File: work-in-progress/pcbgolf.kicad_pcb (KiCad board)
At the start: 4 copper layers, 45 x 37 mm, 239 parts, among them J1 DCBARRELSMT, J2 MICRO_SD-0472192001, J3 USB4105-GF-A, J4 CAN, J5 USB-C-FEMALEGCT, J6 USB-C-FEMALEGCT, J7 USB-C-FEMALEGCT, J8 USB-C-FEMALEGCT, Q1 SIS427-VI, Q2 NFET-DUAL-COMMON-SOURCE-QS5K2, Q3 NFET-DUAL-COMMON-SOURCE-QS5K2, Q4 NFET-DUAL-COMMON-SOURCE-QS5K2, Q5 NFET-DUAL-COMMON-SOURCE-QS5K2, Q6 NFET-DUAL-COMMON-SOURCE-QS5K2, Q7 NFET-DUAL-COMMON-SOURCE-QS5K2, Q8 NFET-DUAL-COMMON-SOURCE-QS5K2, Q9 NFET-DUAL-COMMON-SOURCE-QS5K2, SW1 SPST-2-4PIN, U1 AP62300, U10 NCS20071XV53T2G, U11 NCS20071XV53T2G, U12 NCS20071XV53T2G, U13 TPS25944A, U14 TPS25944A, U15 TPS25944A, U16 TPS25944A, U2 AP62300, U3 STM32H725VGH6, U4 USB2517, U5 MCP2542FDT-E/MNY, U6 MCP2542FDT-E/MNY, U7 MCP2542FDT-E/MNY, U8 MCP2542FDT-E/MNY, U9 NCS20071XV53T2G, Y1 25MHz, Y2 24MHz

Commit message: Advance solo completion to a checked 220-connection WIP
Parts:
- moved Y1 6.91 mm to (3.60, 15.3), turned to 180 degrees
- moved C19 6.40 mm to (4.05, 24.3)
- moved C14 2.97 mm to (3.60, 17.4), turned to 0 degrees
- moved C17 2.33 mm to (1.00, 16.3), turned to 90 degrees
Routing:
- net GND: track 22.2 -> 178.6 mm, vias 57 -> 154
- net CAN1_L: track 0.00 -> 86.8 mm, vias 0 -> 8
- net CAN3_L: track 0.00 -> 76.8 mm, vias 0 -> 5
- net CAN1_H: track 0.00 -> 67.3 mm, vias 0 -> 4
- net CAN0_H: track 0.00 -> 66.6 mm, vias 0 -> 7
- net CAN0_L: track 0.00 -> 52.9 mm, vias 0 -> 4
- net CAN3_H: track 0.00 -> 52.2 mm, vias 0 -> 5
- net Net-(U9--): track 0.00 -> 51.5 mm, vias 0 -> 5
- net BTN: track 1.60 -> 51.0 mm, vias 0 -> 2
- net Net-(Q9-D1): track 0.00 -> 48.4 mm, vias 0 -> 4
- net Net-(Q5-D1): track 0.00 -> 39.6 mm, vias 0 -> 3
- net CAN2_H: track 0.00 -> 37.8 mm, vias 0 -> 4
- net CH4_SBU2_RELAY: track 0.57 -> 36.2 mm, vias 1 -> 2
- net Net-(U3-PC0): track 0.57 -> 34.7 mm
- net CH3_SBU1_RELAY: track 0.57 -> 34.7 mm, vias 1 -> 2
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
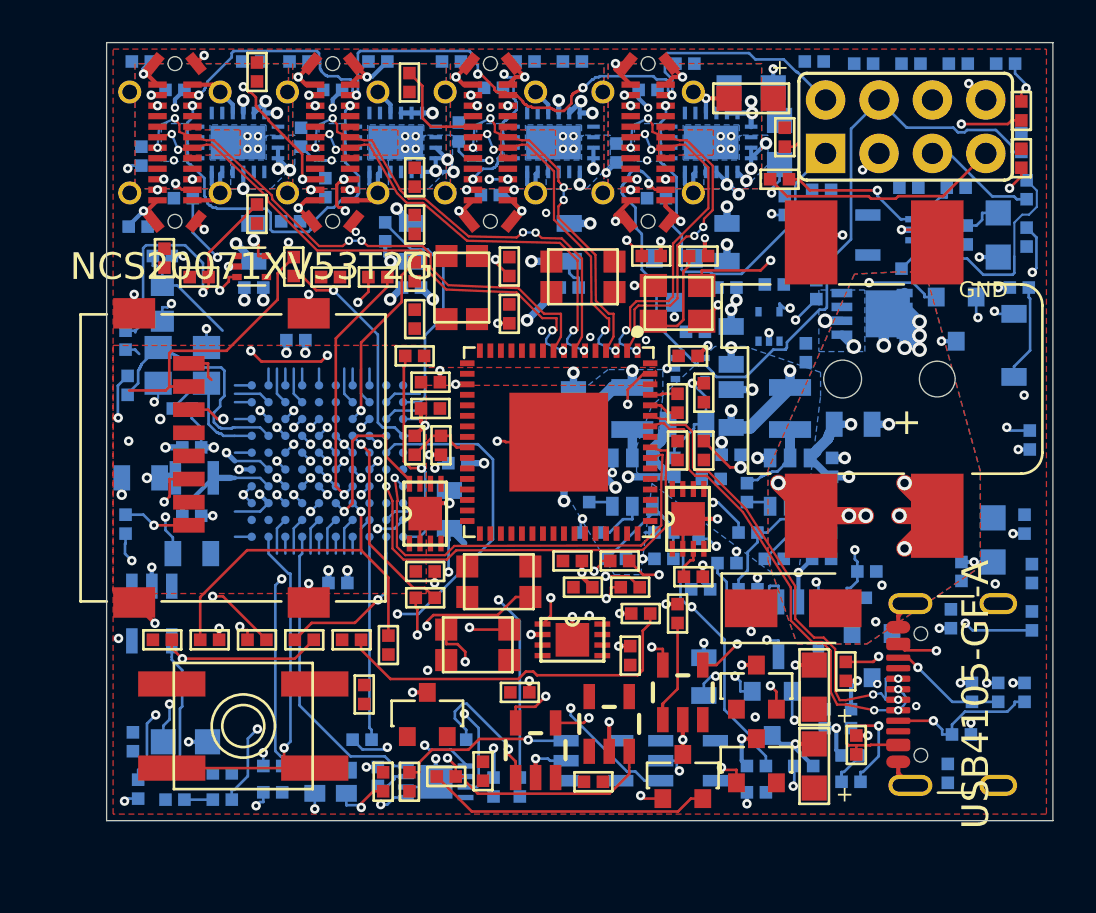
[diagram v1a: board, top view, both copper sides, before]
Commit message: Hand off latest four-layer PCB, routing artifacts and completion plan
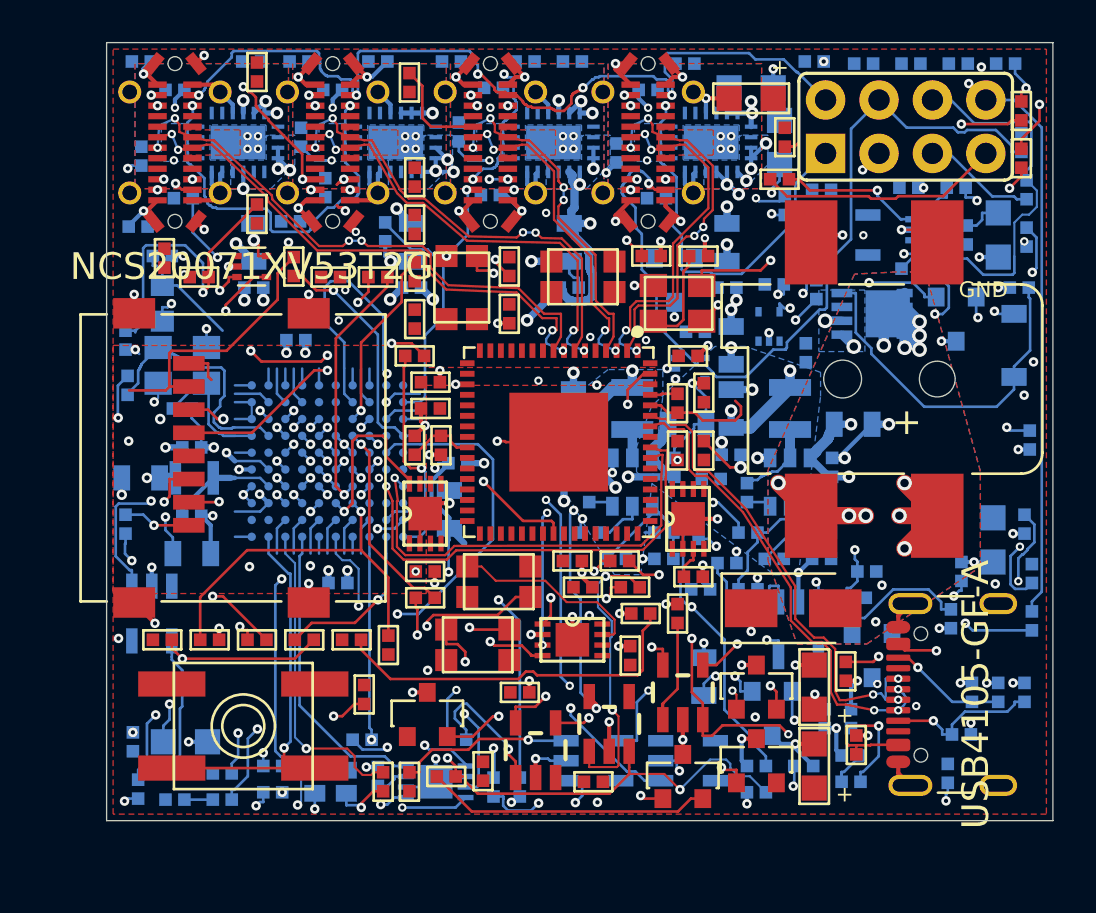
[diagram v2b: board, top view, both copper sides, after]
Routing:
- net Net-(Q6-D2): track 0.00 -> 42.9 mm, vias 0 -> 7
- net CH3_SBU2_IGN: track 17.3 -> 57.7 mm, vias 2 -> 4
- net Net-(LED4-PadA): track 0.00 -> 40.3 mm, vias 0 -> 2
- net +5V: track 19.4 -> 51.7 mm, vias 6 -> 12
- net CH4_SBU1_RELAY: track 18.7 -> 50.3 mm, vias 2 -> 5
- net CAN0_L: track 52.9 -> 83.9 mm, vias 4 -> 7
- net CH4_SBU1: track 0.00 -> 28.3 mm, vias 0 -> 3
- net Net-(Q8-D1): track 0.00 -> 28.3 mm, vias 0 -> 4
- net Net-(R62-Pad1): track 0.00 -> 27.8 mm, vias 0 -> 4
- net Net-(LED15-AG): track 0.00 -> 27.1 mm, vias 0 -> 3
- net CAN3_H: track 52.2 -> 78.6 mm
- net HUB_SDA: track 1.77 -> 24.1 mm, vias 0 -> 2
- net CH2_SBU2_IGN: track 1.77 -> 22.0 mm, vias 0 -> 2
- net CH1_SBU1: track 0.00 -> 19.3 mm, vias 0 -> 3
- net Net-(U11-+): track 0.00 -> 17.3 mm, vias 0 -> 2
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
